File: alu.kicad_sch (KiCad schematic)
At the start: 41 parts, among them J0 640-USB4970-00-A, SW0 SW_DIP_x04, SW1 SW_DIP_x04, SW2 SW_DIP_x04, U0 SN74LS08N, U1 SN74HC86N, U2 SN74HC86N, U3 SN74LS08N, U4 SN74LS08N, U5 CD74HCT32E

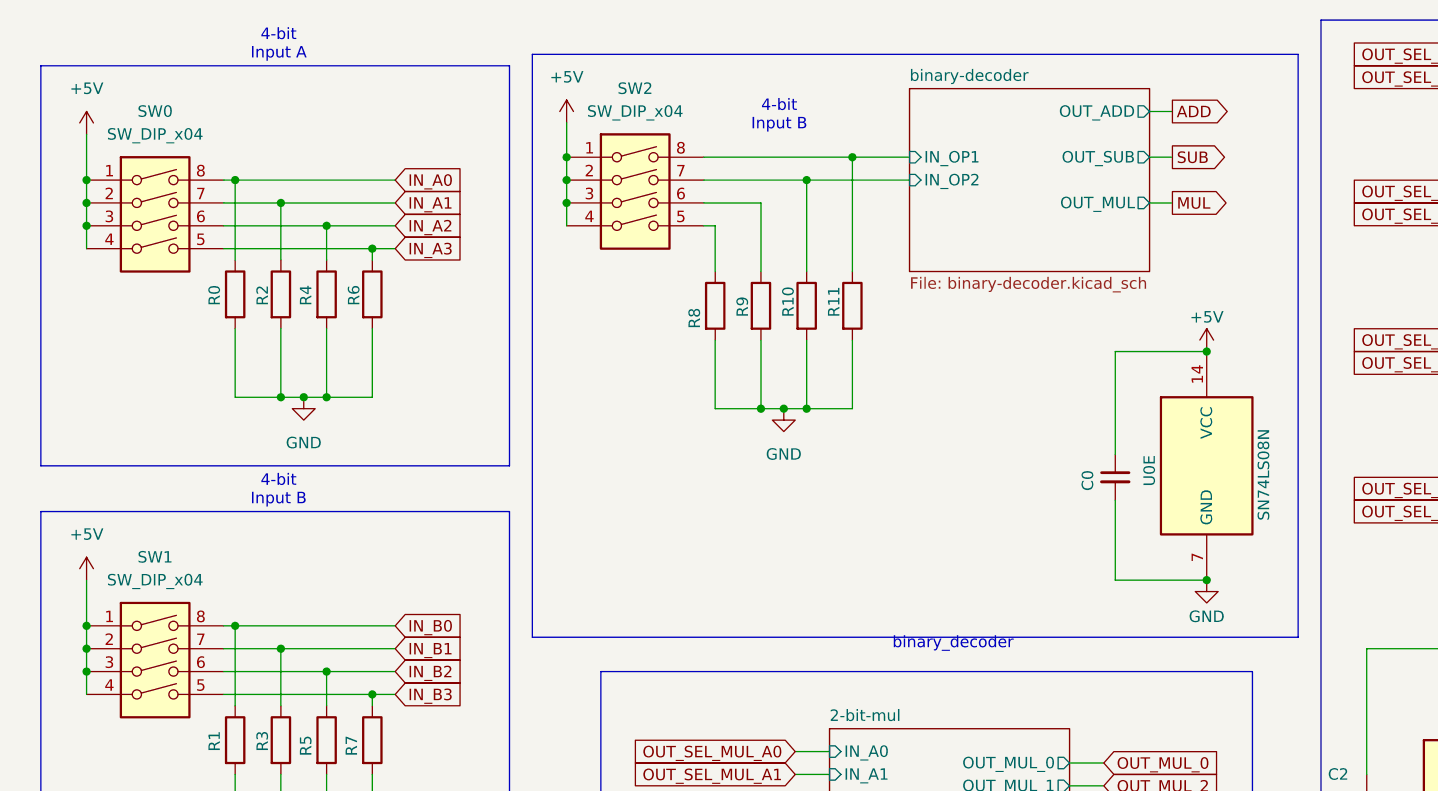
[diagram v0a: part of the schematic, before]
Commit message: fix: change dip switch footprint
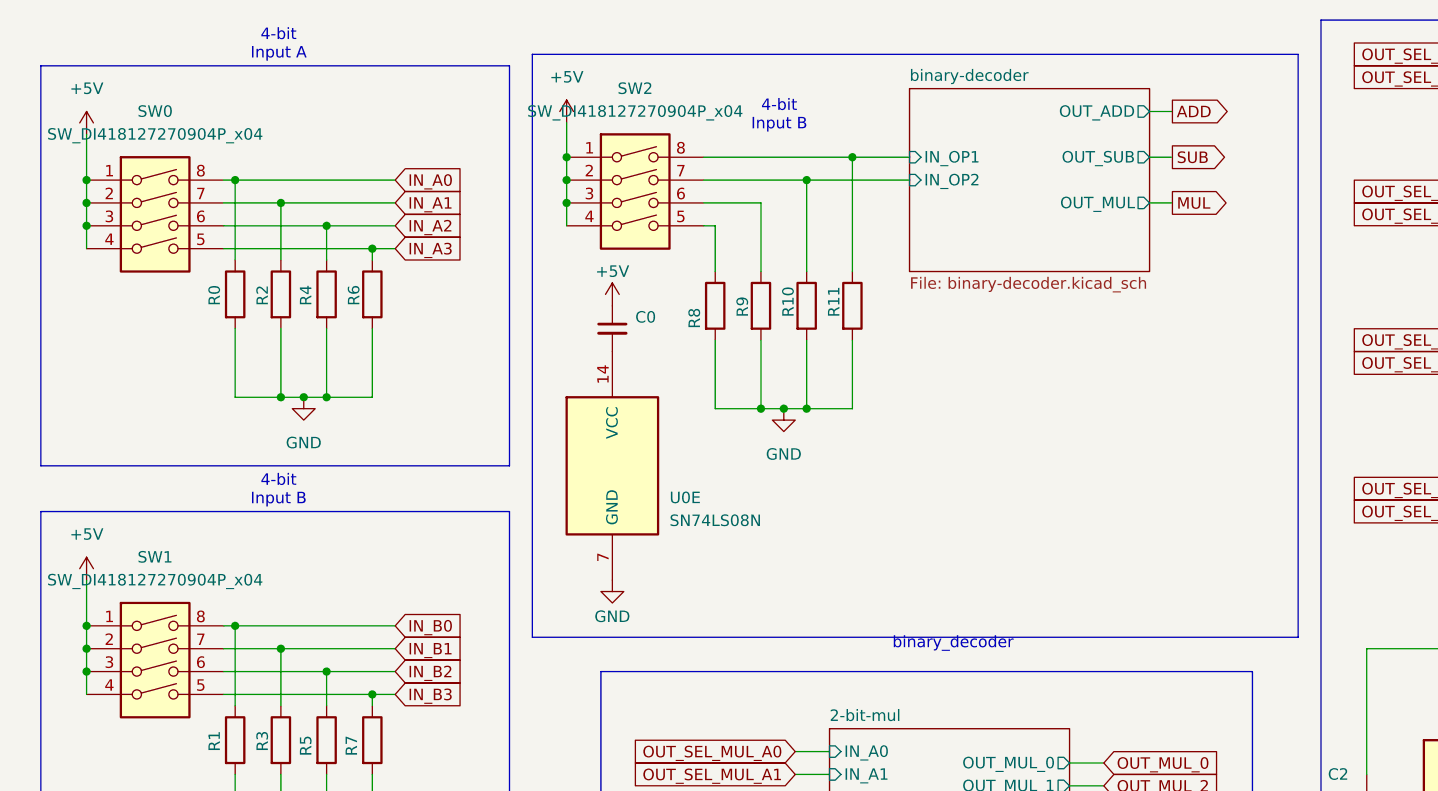
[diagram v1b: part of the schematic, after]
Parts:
- SW0, SW1, SW2: value SW_DIP_x04 -> SW_DI418127270904P_x04; footprint Package_DIP:DIP-4_W7.62mm_LongPads -> Package_DIP:DIP-8_W7.62mm_LongPads
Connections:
- net +5V: no longer U0.14 (VCC)
- net GND: no longer C0.2
- new net: C0.2, U0.14 (VCC)
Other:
- moved on the sheet: C0, U0E
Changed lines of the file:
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@@
 	)
 	(junction
-		(at 149.86 74.93)
-		(diameter 0)
-		(color 0 0 0 0)
-	)
-	(junction
 		(at 105.41 30.48)
 		(diameter 0)
@@
 	)
 	(junction
-		(at 149.86 49.53)
-		(diameter 0)
-		(color 0 0 0 0)
-	)
-	(junction
 		(at 267.97 137.16)
 		(diameter 0)
@@
 	(wire
 		(pts
-			(xy 139.7 66.04) (xy 139.7 74.93)
-		)
-		(stroke
-			(width 0)
-			(type default)
-		)
-	)
-	(wire
-		(pts
 			(xy 41.91 46.99) (xy 41.91 54.61)
 		)
@@
 	(wire
 		(pts
-			(xy 149.86 49.53) (xy 139.7 49.53)
-		)
-		(stroke
-			(width 0)
-			(type default)
-		)
-	)
-	(wire
-		(pts
 			(xy 184.15 16.51) (xy 186.69 16.51)
 		)
@@
 	(wire
 		(pts
-			(xy 139.7 49.53) (xy 139.7 60.96)
-		)
-		(stroke
-			(width 0)
-			(type default)
-		)
-	)
-	(wire
-		(pts
 			(xy 231.14 82.55) (xy 231.14 97.79)
 		)
@@
 	(wire
 		(pts
-			(xy 139.7 74.93) (xy 149.86 74.93)
-		)
-		(stroke
-			(width 0)
-			(type default)
-		)
-	)
-	(wire
-		(pts
 			(xy 46.99 88.9) (xy 46.99 82.55)
 		)
@@
 	(symbol
 		(lib_id "power:GND")
-		(at 149.86 74.93 0)
+		(at 83.82 74.93 0)
 		(unit 1)
 		(body_style 1)
@@
 		(dnp no)
 		(property "Reference" "#PWR06"
-			(at 149.86 81.28 0)
+			(at 83.82 81.28 0)
 			(hide yes)
 			(show_name no)
@@
 		)
 		(property "Value" "GND"
-			(at 149.86 78.994 0)
+			(at 83.82 78.994 0)
 			(show_name no)
 			(do_not_autoplace no)
@@
 		)
 		(property "Footprint" ""
-			(at 149.86 74.93 0)
+			(at 83.82 74.93 0)
 			(hide yes)
 			(show_name no)
@@
 		)
 		(property "Datasheet" ""
-			(at 149.86 74.93 0)
+			(at 83.82 74.93 0)
 			(hide yes)
 			(show_name no)
@@
 		)
 		(property "Description" "Power symbol creates a global label with name \"GND\" , ground"
-			(at 149.86 74.93 0)
+			(at 83.82 74.93 0)
 			(hide yes)
 			(show_name no)
@@
 			)
 		)
-		(property "Value" "SW_DIP_x04"
+		(property "Value" "SW_DI418127270904P_x04"
 			(at 33.02 25.4 0)
 			(show_name no)
@@
 			)
 		)
-		(property "Footprint" "Package_DIP:DIP-4_W7.62mm_LongPads"
+		(property "Footprint" "Package_DIP:DIP-8_W7.62mm_LongPads"
 			(at 33.02 35.56 0)
 			(hide yes)
@@
 			)
 		)
-		(property "Value" "SW_DIP_x04"
+		(property "Value" "SW_DI418127270904P_x04"
 			(at 86.36 22.86 0)
 			(show_name no)
@@
 			)
 		)
-		(property "Footprint" "Package_DIP:DIP-4_W7.62mm_LongPads"
+		(property "Footprint" "Package_DIP:DIP-8_W7.62mm_LongPads"
 			(at 86.36 33.02 0)
 			(hide yes)
@@
 	(symbol
 		(lib_id "74xx:74LS08")
-		(at 149.86 62.23 0)
+		(at 83.82 62.23 0)
 		(unit 5)
 		(body_style 1)
@@
 		(dnp no)
 		(property "Reference" "U0"
-			(at 143.51 64.516 90)
+			(at 90.17 65.786 0)
 			(show_name no)
 			(do_not_autoplace no)
@@
 		)
 		(property "Value" "SN74LS08N"
-			(at 156.21 68.326 90)
+			(at 90.17 68.326 0)
 			(show_name no)
 			(do_not_autoplace no)
@@
 		)
 		(property "Footprint" "Package_DIP:DIP-14_W7.62mm_LongPads"
-			(at 149.86 62.23 0)
+			(at 83.82 62.23 0)
 			(hide yes)
 			(show_name no)
@@
 		)
 		(property "Datasheet" "https://www.ti.com/lit/ds/symlink/sn74hc86.pdf"
-			(at 149.86 62.23 0)
+			(at 83.82 62.23 0)
 			(hide yes)
 			(show_name no)
@@
 		)
 		(property "Description" "Quad And2"
-			(at 149.86 62.23 0)
+			(at 83.82 62.23 0)
 			(hide yes)
 			(show_name no)
@@
 	(symbol
 		(lib_id "power:+5V")
-		(at 149.86 49.53 0)
+		(at 83.82 44.45 0)
 		(unit 1)
 		(body_style 1)
@@
 		(dnp no)
 		(property "Reference" "#PWR05"
-			(at 149.86 53.34 0)
+			(at 83.82 48.26 0)
 			(hide yes)
 			(show_name no)
@@
 		)
 		(property "Value" "+5V"
-			(at 149.86 45.72 0)
+			(at 83.82 40.64 0)
 			(show_name no)
 			(do_not_autoplace no)
@@
 		)
 		(property "Footprint" ""
-			(at 149.86 49.53 0)
+			(at 83.82 44.45 0)
 			(hide yes)
 			(show_name no)
@@
 		)
 		(property "Datasheet" ""
-			(at 149.86 49.53 0)
+			(at 83.82 44.45 0)
 			(hide yes)
 			(show_name no)
@@
 		)
 		(property "Description" "Power symbol creates a global label with name \"+5V\""
-			(at 149.86 49.53 0)
+			(at 83.82 44.45 0)
 			(hide yes)
 			(show_name no)
@@
 			)
 		)
-		(property "Value" "SW_DIP_x04"
+		(property "Value" "SW_DI418127270904P_x04"
 			(at 33.02 74.93 0)
 			(show_name no)
@@
 			)
 		)
-		(property "Footprint" "Package_DIP:DIP-4_W7.62mm_LongPads"
+		(property "Footprint" "Package_DIP:DIP-8_W7.62mm_LongPads"
 			(at 33.02 85.09 0)
 			(hide yes)
@@
 	(symbol
 		(lib_id "Device:C_Small")
-		(at 139.7 63.5 0)
+		(at 83.82 46.99 0)
 		(unit 1)
 		(body_style 1)
@@
 		(in_pos_files yes)
 		(dnp no)
+		(fields_autoplaced yes)
 		(property "Reference" "C0"
-			(at 136.652 65.024 90)
+			(at 86.36 45.7262 0)
 			(show_name no)
 			(do_not_autoplace no)
@@
 		)
 		(property "Value" "CC0603KRX7R9BB104"
-			(at 142.24 64.7762 0)
+			(at 86.36 48.2662 0)
 			(hide yes)
 			(show_name no)
@@
 		)
 		(property "Footprint" "Capacitor_SMD:C_0603_1608Metric_Pad1.08x0.95mm_HandSolder"
-			(at 139.7 63.5 0)
+			(at 83.82 46.99 0)
 			(hide yes)
 			(show_name no)
@@
 		)
 		(property "Datasheet" ""
-			(at 139.7 63.5 0)
+			(at 83.82 46.99 0)
 			(hide yes)
 			(show_name no)
@@
 		)
 		(property "Description" "Unpolarized capacitor, small symbol"
-			(at 139.7 63.5 0)
+			(at 83.82 46.99 0)
 			(hide yes)
 			(show_name no)

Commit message: feat: updated references
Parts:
- R0, R1, R10, R11, R2, R3, R4, R5, R6, R7, R8, R9: value CRG0603J10K - 3399584 -> RC0603FR-07220RL
- SW0, SW1, SW2: value SW_DI418127270904P_x04 -> 418127270904
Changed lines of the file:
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@@
 			)
 		)
-		(property "Value" "CRG0603J10K - 3399584"
+		(property "Value" "RC0603FR-07220RL"
 			(at 102.87 45.7199 0)
 			(hide yes)
@@
 			)
 		)
-		(property "Value" "CRG0603J10K - 3399584"
+		(property "Value" "RC0603FR-07220RL"
 			(at 113.03 45.7199 0)
 			(hide yes)
@@
 			)
 		)
-		(property "Value" "CRG0603J10K - 3399584"
+		(property "Value" "RC0603FR-07220RL"
 			(at 44.45 44.4499 0)
 			(hide yes)
@@
 			)
 		)
-		(property "Value" "CRG0603J10K - 3399584"
+		(property "Value" "RC0603FR-07220RL"
 			(at 107.95 45.7199 0)
 			(hide yes)
@@
 			)
 		)
-		(property "Value" "SW_DI418127270904P_x04"
+		(property "Value" "418127270904"
 			(at 33.02 25.4 0)
 			(show_name no)
@@
 			)
 		)
-		(property "Value" "SW_DI418127270904P_x04"
+		(property "Value" "418127270904"
 			(at 86.36 22.86 0)
 			(show_name no)
@@
 			)
 		)
-		(property "Value" "CRG0603J10K - 3399584"
+		(property "Value" "RC0603FR-07220RL"
 			(at 59.69 44.4499 0)
 			(hide yes)
@@
 			)
 		)
-		(property "Value" "CRG0603J10K - 3399584"
+		(property "Value" "RC0603FR-07220RL"
 			(at 49.53 93.9799 0)
 			(hide yes)
@@
 			)
 		)
-		(property "Value" "CRG0603J10K - 3399584"
+		(property "Value" "RC0603FR-07220RL"
 			(at 54.61 44.4499 0)
 			(hide yes)
@@
 			)
 		)
-		(property "Value" "CRG0603J10K - 3399584"
+		(property "Value" "RC0603FR-07220RL"
 			(at 59.69 93.9799 0)
 			(hide yes)
@@
 			)
 		)
-		(property "Value" "SW_DI418127270904P_x04"
+		(property "Value" "418127270904"
 			(at 33.02 74.93 0)
 			(show_name no)
@@
 			)
 		)
-		(property "Value" "CRG0603J10K - 3399584"
+		(property "Value" "RC0603FR-07220RL"
 			(at 49.53 44.4499 0)
 			(hide yes)
@@
 			)
 		)
-		(property "Value" "CRG0603J10K - 3399584"
+		(property "Value" "RC0603FR-07220RL"
 			(at 54.61 93.9799 0)
 			(hide yes)
@@
 			)
 		)
-		(property "Value" "CRG0603J10K - 3399584"
+		(property "Value" "RC0603FR-07220RL"
 			(at 44.45 93.9799 0)
 			(hide yes)
@@
 			)
 		)
-		(property "Value" "CRG0603J10K - 3399584"
+		(property "Value" "RC0603FR-07220RL"
 			(at 97.79 45.7199 0)
 			(hide yes)
